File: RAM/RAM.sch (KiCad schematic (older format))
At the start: 15 parts, among them J1 Conn_01x08_Male, J2 Conn_01x08_Male, J3 Conn_01x08_Male, J4 Conn_01x05_Male, J5 Conn_01x08_Male, U1 74LS283, U2 CY62256-70PC, U3 74LS283, U4 74LS283, U5 74LS283

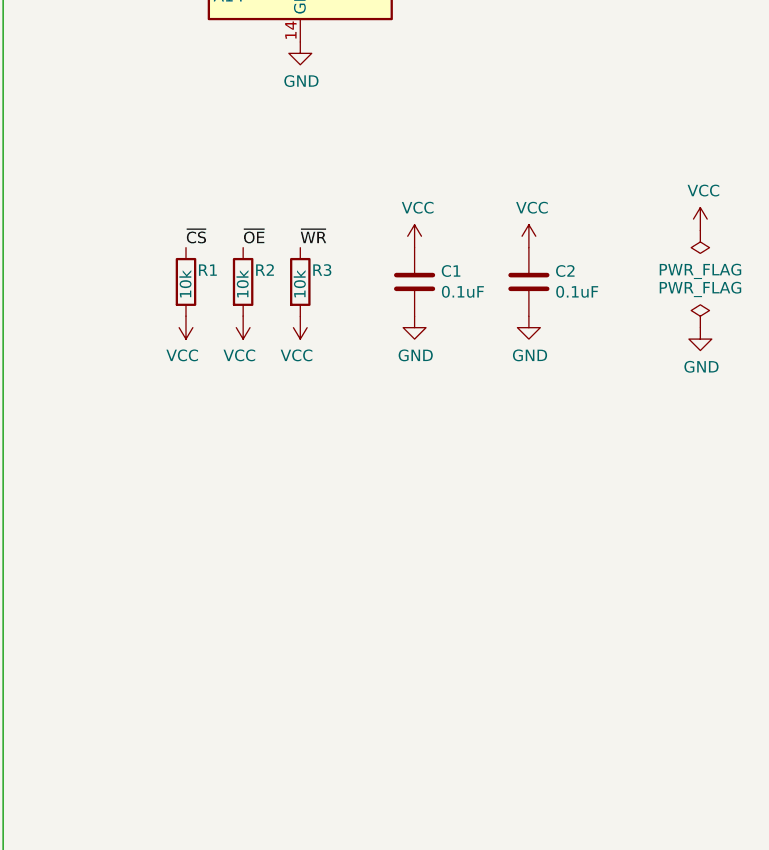
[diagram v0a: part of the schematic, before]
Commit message: Polishing RAM
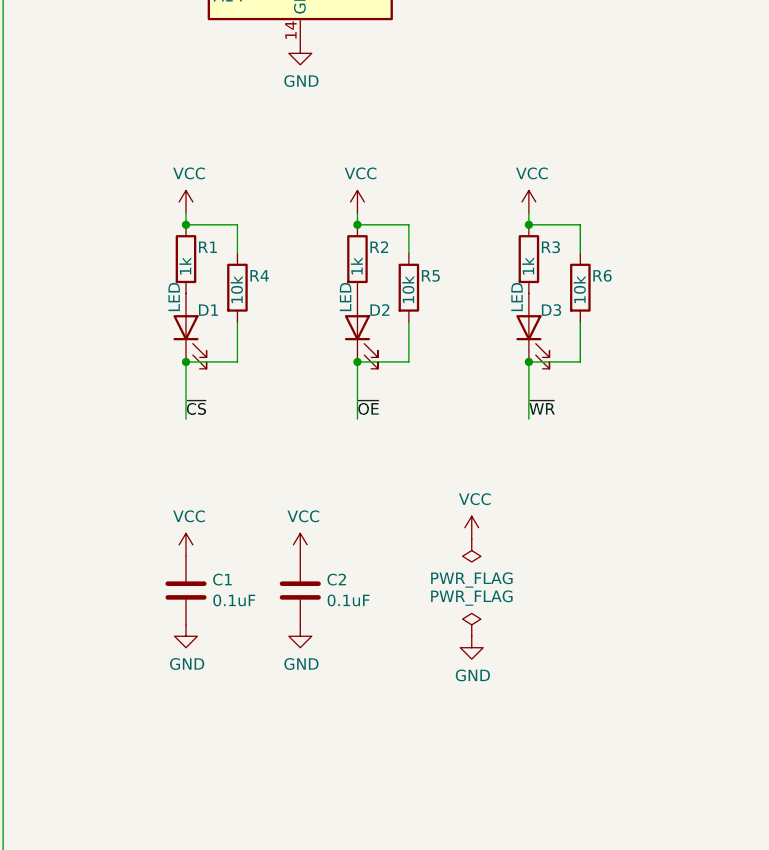
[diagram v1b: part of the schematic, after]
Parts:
- added D1, D2, D3: LED, LED_SMD:LED_0805_2012Metric_Pad1.15x1.40mm_HandSolder, symbol Device:LED
- added R4, R5, R6: 10k, Resistor_SMD:R_0805_2012Metric_Pad1.20x1.40mm_HandSolder, symbol Device:R
- R1, R2, R3: value 10k -> 1k
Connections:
- net VCC: now also R1.1, R2.1, R3.1, R4.1, R5.1, R6.1; no longer R1.2, R2.2, R3.2
- net ~CS: now also D1.1 (K), R4.2; no longer R1.1
- net ~OE: now also D2.1 (K), R5.2; no longer R2.1
- net ~WR: now also D3.1 (K), R6.2; no longer R3.1
- new net: D1.2 (A), R1.2
- new net: D2.2 (A), R2.2
- new net: D3.2 (A), R3.2
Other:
- moved on the sheet: C1, C2, R1, R2, R3

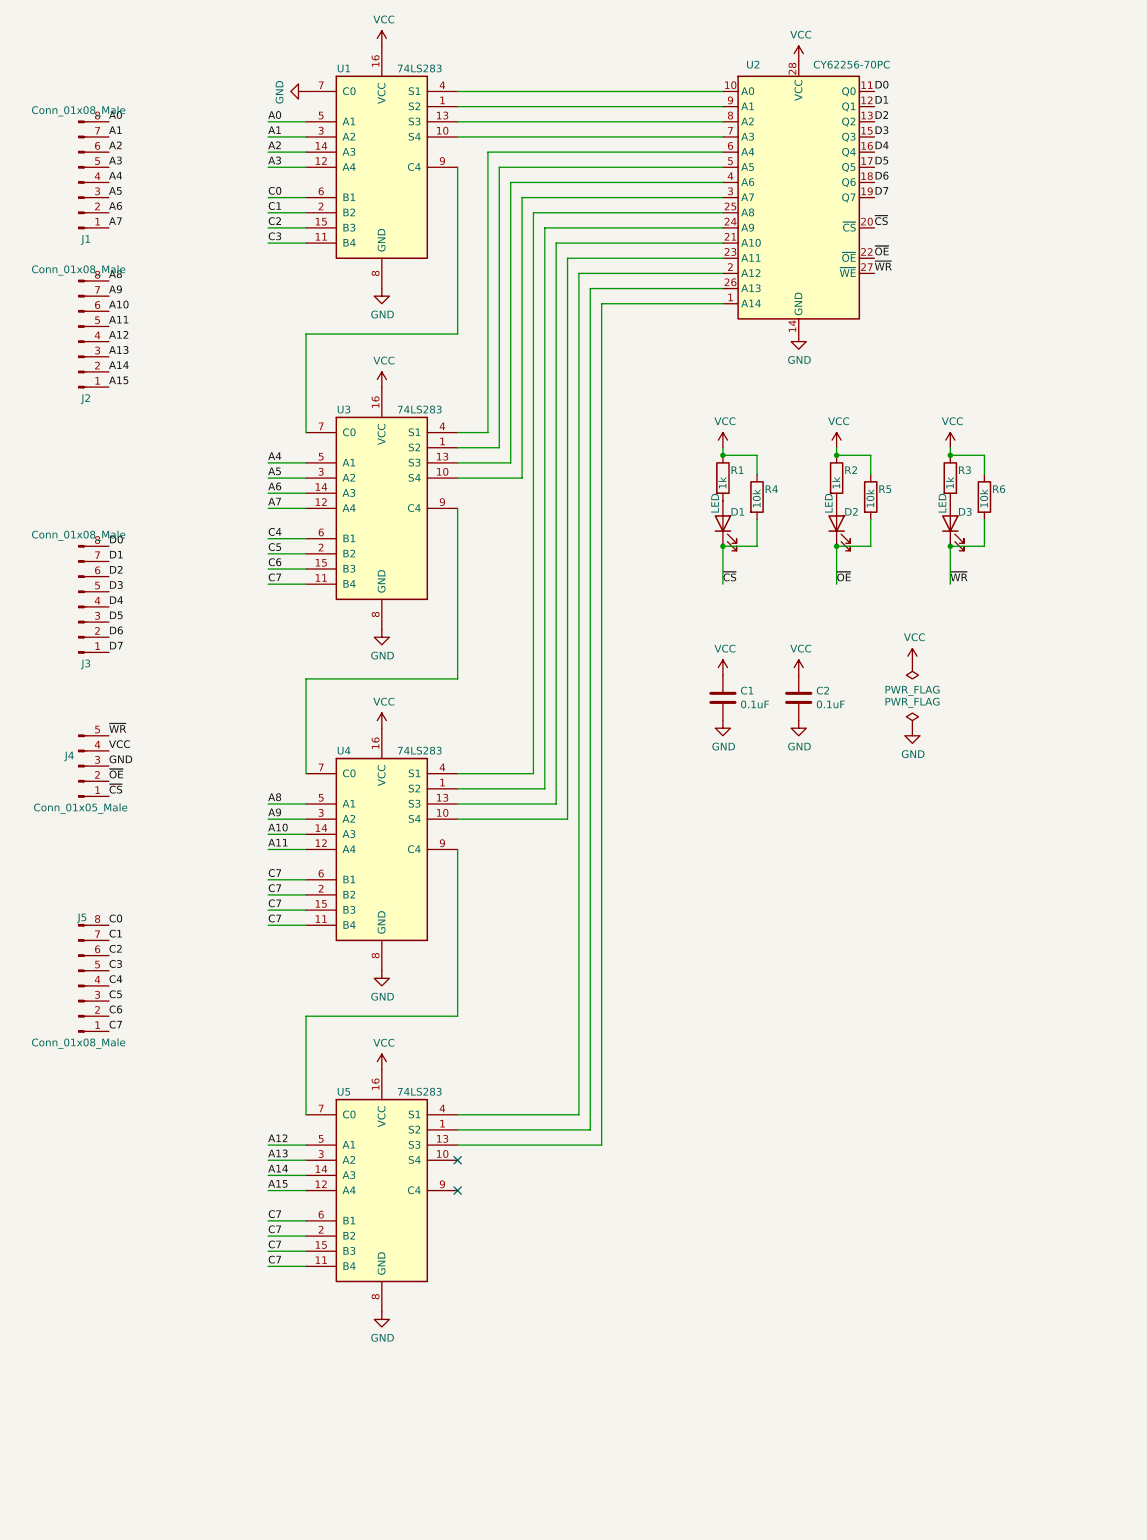
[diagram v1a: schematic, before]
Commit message: Try to add ROM to RAM
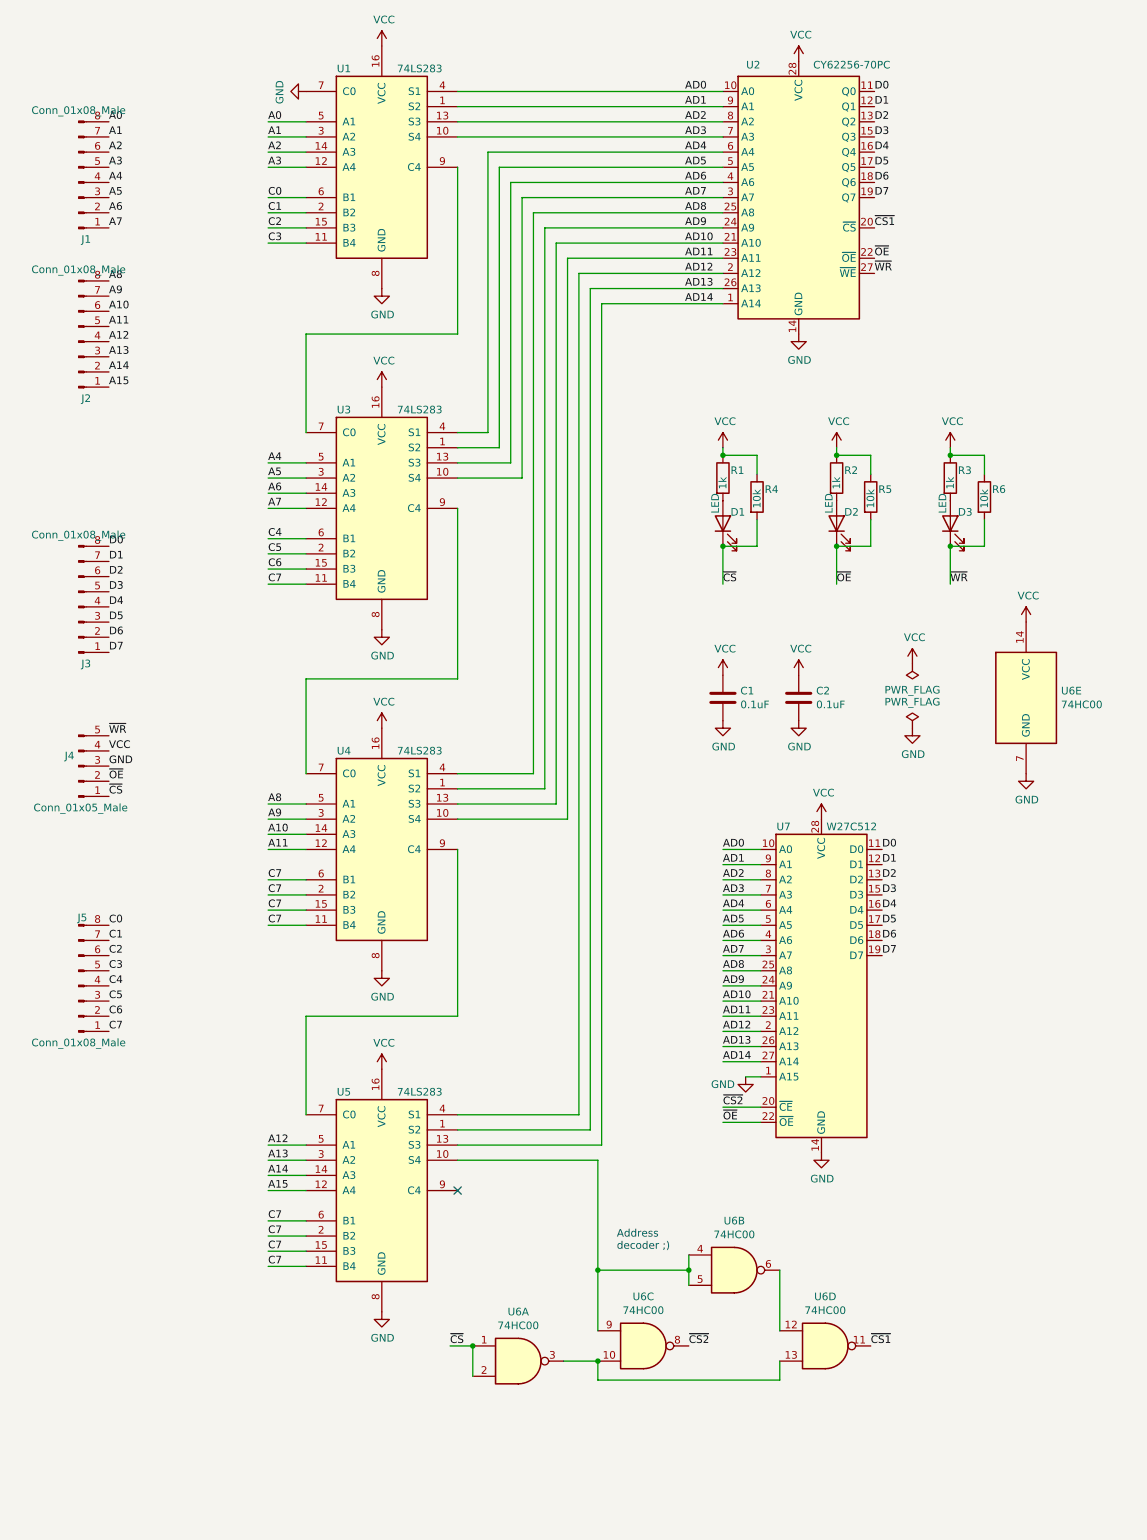
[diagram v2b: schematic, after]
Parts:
- added U6: 74HC00, Package_DIP:DIP-14_W7.62mm, symbol 74xx:74HC00
- added U7: W27C512, Package_DIP:DIP-28_W15.24mm, symbol Memory_EPROM:27C512
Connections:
- net D0: now also U7.11 (D0)
- net D1: now also U7.12 (D1)
- net D2: now also U7.13 (D2)
- net D3: now also U7.15 (D3)
- net D4: now also U7.16 (D4)
- net D5: now also U7.17 (D5)
- net D6: now also U7.18 (D6)
- net D7: now also U7.19 (D7)
- net GND: now also U6.7 (GND), U7.1 (A15), U7.14 (GND)
- net VCC: now also U6.14 (VCC), U7.28 (VCC)
- net ~CS: now also U6.1, U6.2; no longer U2.20 (~CS)
- net ~OE: now also U7.22 (~OE)
- net AD14: now reaches U2.1 (A14), U5.13 (S3)
- net AD14: now also U7.27 (A14)
- net AD0: now reaches U1.4 (S1), U2.10 (A0)
- net AD0: now also U7.10 (A0)
- net AD12: now reaches U2.2 (A12), U5.4 (S1)
- net AD12: now also U7.2 (A12)
- net AD10: now reaches U2.21 (A10), U4.13 (S3)
- net AD10: now also U7.21 (A10)
- net AD11: now reaches U2.23 (A11), U4.10 (S4)
- net AD11: now also U7.23 (A11)
- net AD9: now reaches U2.24 (A9), U4.1 (S2)
- net AD9: now also U7.24 (A9)
- net AD8: now reaches U2.25 (A8), U4.4 (S1)
- net AD8: now also U7.25 (A8)
- net AD13: now reaches U2.26 (A13), U5.1 (S2)
- net AD13: now also U7.26 (A13)
- net AD7: now reaches U2.3 (A7), U3.10 (S4)
- net AD7: now also U7.3 (A7)
- net AD6: now reaches U2.4 (A6), U3.13 (S3)
- net AD6: now also U7.4 (A6)
- net AD5: now reaches U2.5 (A5), U3.1 (S2)
- net AD5: now also U7.5 (A5)
- net AD4: now reaches U2.6 (A4), U3.4 (S1)
- net AD4: now also U7.6 (A4)
- net AD3: now reaches U1.10 (S4), U2.7 (A3)
- net AD3: now also U7.7 (A3)
- net AD2: now reaches U1.13 (S3), U2.8 (A2)
- net AD2: now also U7.8 (A2)
- net AD1: now reaches U1.1 (S2), U2.9 (A1)
- net AD1: now also U7.9 (A1)
- net at U5.10 (S4): now also U6.4, U6.5, U6.9
- new net: U6.10, U6.13, U6.3
- new net: U6.12, U6.6
- new net ~CS1: U2.20 (~CS), U6.11
- new net ~CS2: U6.8, U7.20 (~CE)
- no-connect marks 2 -> 1
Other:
- note added: "Address\ndecoder ;)"

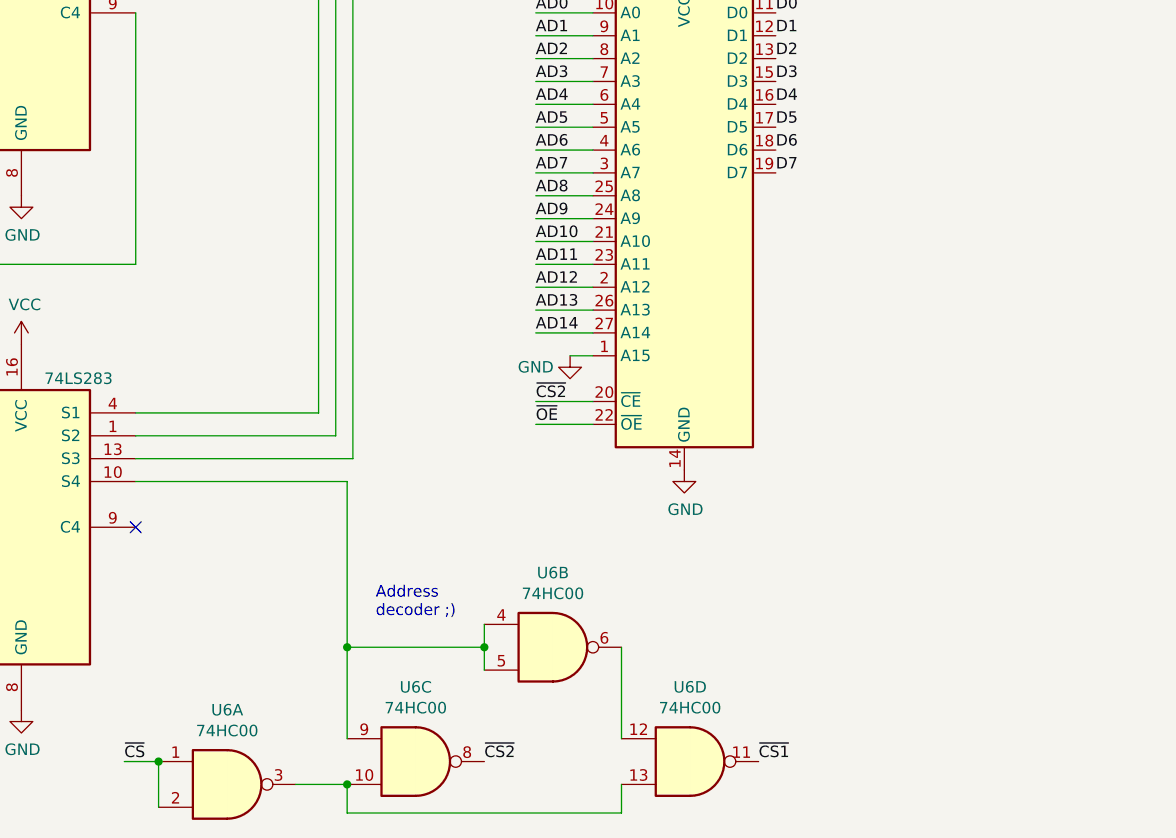
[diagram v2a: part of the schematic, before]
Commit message: Try to add ROM to RAM
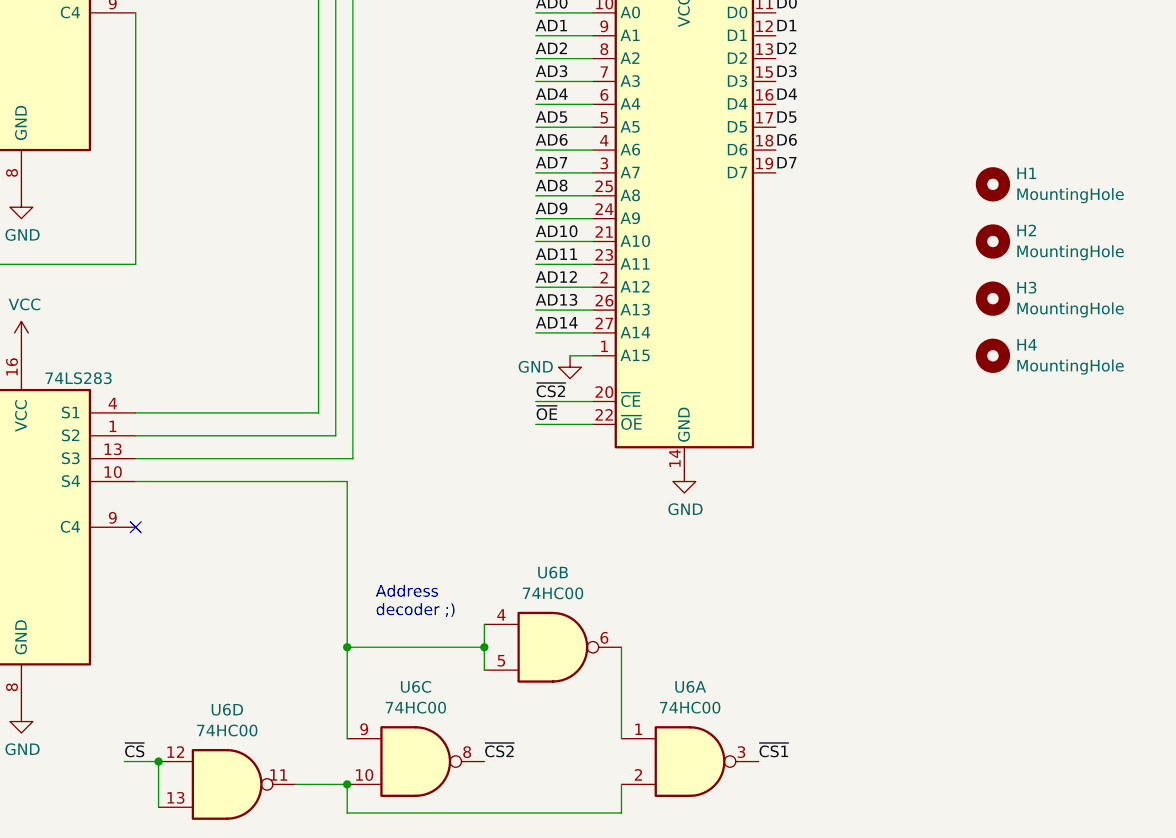
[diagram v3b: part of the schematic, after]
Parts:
- added H1, H2, H3, H4: MountingHole, MountingHole:MountingHole_3.2mm_M3, symbol Mechanical:MountingHole
- D1, D2, D3: footprint LED_SMD:LED_0805_2012Metric_Pad1.15x1.40mm_HandSolder -> LED_THT:LED_Rectangular_W5.0mm_H2.0mm
- J1, J2, J3: footprint Connector_PinHeader_2.54mm:PinHeader_1x08_P2.54mm_Horizontal -> Connector_PinHeader_2.54mm:PinHeader_1x08_P2.54mm_Vertical
- J4: footprint Connector_PinHeader_2.54mm:PinHeader_1x05_P2.54mm_Horizontal -> Connector_PinHeader_2.54mm:PinHeader_1x05_P2.54mm_Vertical
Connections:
- net ~CS: now also U6.12, U6.13; no longer U6.1, U6.2
- net ~CS1: now also U6.3; no longer U6.11
- net at U6.6: now also U6.1; no longer U6.12
- new net: U6.10, U6.11, U6.2
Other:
- moved on the sheet: U6A, U6D
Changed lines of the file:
@@
 F 0 "J1" H 800 2225 50  0000 C CNN
 F 1 "Conn_01x08_Male" H 750 1375 50  0000 C CNN
-F 2 "Connector_PinHeader_2.54mm:PinHeader_1x08_P2.54mm_Horizontal" H 750 1850 50  0001 C CNN
+F 2 "Connector_PinHeader_2.54mm:PinHeader_1x08_P2.54mm_Vertical" H 750 1850 50  0001 C CNN
 F 3 "~" H 750 1850 50  0001 C CNN
 	1    750  1850
@@
 F 0 "J2" H 800 3275 50  0000 C CNN
 F 1 "Conn_01x08_Male" H 750 2425 50  0000 C CNN
-F 2 "Connector_PinHeader_2.54mm:PinHeader_1x08_P2.54mm_Horizontal" H 750 2900 50  0001 C CNN
+F 2 "Connector_PinHeader_2.54mm:PinHeader_1x08_P2.54mm_Vertical" H 750 2900 50  0001 C CNN
 F 3 "~" H 750 2900 50  0001 C CNN
 	1    750  2900
@@
 F 0 "J3" H 800 5025 50  0000 C CNN
 F 1 "Conn_01x08_Male" H 750 4175 50  0000 C CNN
-F 2 "Connector_PinHeader_2.54mm:PinHeader_1x08_P2.54mm_Horizontal" H 750 4650 50  0001 C CNN
+F 2 "Connector_PinHeader_2.54mm:PinHeader_1x08_P2.54mm_Vertical" H 750 4650 50  0001 C CNN
 F 3 "~" H 750 4650 50  0001 C CNN
 	1    750  4650
@@
 F 0 "J4" H 722 5632 50  0000 R CNN
 F 1 "Conn_01x05_Male" H 1075 5975 50  0000 R CNN
-F 2 "Connector_PinHeader_2.54mm:PinHeader_1x05_P2.54mm_Horizontal" H 750 5700 50  0001 C CNN
+F 2 "Connector_PinHeader_2.54mm:PinHeader_1x05_P2.54mm_Vertical" H 750 5700 50  0001 C CNN
 F 3 "~" H 750 5700 50  0001 C CNN
 	1    750  5700
@@
 F 0 "D1" V 5075 4050 50  0000 R CNN
 F 1 "LED" H 5200 4150 50  0000 R CNN
-F 2 "LED_SMD:LED_0805_2012Metric_Pad1.15x1.40mm_HandSolder" H 5000 4100 50  0001 C CNN
+F 2 "LED_THT:LED_Rectangular_W5.0mm_H2.0mm" H 5000 4100 50  0001 C CNN
 F 3 "~" H 5000 4100 50  0001 C CNN
 	1    5000 4100
@@
 F 0 "D2" V 5825 4050 50  0000 R CNN
 F 1 "LED" H 5950 4150 50  0000 R CNN
-F 2 "LED_SMD:LED_0805_2012Metric_Pad1.15x1.40mm_HandSolder" H 5750 4100 50  0001 C CNN
+F 2 "LED_THT:LED_Rectangular_W5.0mm_H2.0mm" H 5750 4100 50  0001 C CNN
 F 3 "~" H 5750 4100 50  0001 C CNN
 	1    5750 4100
@@
 F 0 "D3" V 6575 4050 50  0000 R CNN
 F 1 "LED" H 6700 4150 50  0000 R CNN
-F 2 "LED_SMD:LED_0805_2012Metric_Pad1.15x1.40mm_HandSolder" H 6500 4100 50  0001 C CNN
+F 2 "LED_THT:LED_Rectangular_W5.0mm_H2.0mm" H 6500 4100 50  0001 C CNN
 F 3 "~" H 6500 4100 50  0001 C CNN
 	1    6500 4100
@@
 L 74xx:74HC00 U6
 U 1 1 6495168F
-P 3650 9625
-F 0 "U6" H 3650 9950 50  0000 C CNN
-F 1 "74HC00" H 3650 9859 50  0000 C CNN
-F 2 "Package_DIP:DIP-14_W7.62mm" H 3650 9625 50  0001 C CNN
-F 3 "http://www.ti.com/lit/gpn/sn74hc00" H 3650 9625 50  0001 C CNN
-	1    3650 9625
+P 5675 9525
+F 0 "U6" H 5675 9850 50  0000 C CNN
+F 1 "74HC00" H 5675 9759 50  0000 C CNN
+F 2 "Package_DIP:DIP-14_W7.62mm" H 5675 9525 50  0001 C CNN
+F 3 "http://www.ti.com/lit/gpn/sn74hc00" H 5675 9525 50  0001 C CNN
+	1    5675 9525
 	1    0    0    -1
 $EndComp
@@
 L 74xx:74HC00 U6
 U 4 1 64956F5A
-P 5675 9525
-F 0 "U6" H 5675 9850 50  0000 C CNN
-F 1 "74HC00" H 5675 9759 50  0000 C CNN
-F 2 "Package_DIP:DIP-14_W7.62mm" H 5675 9525 50  0001 C CNN
-F 3 "http://www.ti.com/lit/gpn/sn74hc00" H 5675 9525 50  0001 C CNN
-	4    5675 9525
+P 3650 9625
+F 0 "U6" H 3650 9950 50  0000 C CNN
+F 1 "74HC00" H 3650 9859 50  0000 C CNN
+F 2 "Package_DIP:DIP-14_W7.62mm" H 3650 9625 50  0001 C CNN
+F 3 "http://www.ti.com/lit/gpn/sn74hc00" H 3650 9625 50  0001 C CNN
+	4    3650 9625
 	1    0    0    -1
 $EndComp
@@
 	4175 9750 5375 9750
 Wire Wire Line
-	5375 9750 5375 9625
-Wire Wire Line
 	3950 9625 4175 9625
 Connection ~ 4175 9625
@@
 Text Notes 4300 8900 0    50   ~ 0
 Address\ndecoder ;)
+$Comp
+L Mechanical:MountingHole H1
+U 1 1 64922E67
+P 7000 7000
+F 0 "H1" H 7100 7046 50  0000 L CNN
+F 1 "MountingHole" H 7100 6955 50  0000 L CNN
+F 2 "MountingHole:MountingHole_3.2mm_M3" H 7000 7000 50  0001 C CNN
+F 3 "~" H 7000 7000 50  0001 C CNN
+	1    7000 7000
+	1    0    0    -1
+$EndComp
+$Comp
+L Mechanical:MountingHole H2
+U 1 1 64923BB4
+P 7000 7250
+F 0 "H2" H 7100 7296 50  0000 L CNN
+F 1 "MountingHole" H 7100 7205 50  0000 L CNN
+F 2 "MountingHole:MountingHole_3.2mm_M3" H 7000 7250 50  0001 C CNN
+F 3 "~" H 7000 7250 50  0001 C CNN
+	1    7000 7250
+	1    0    0    -1
+$EndComp
+$Comp
+L Mechanical:MountingHole H3
+U 1 1 64924557
+P 7000 7500
+F 0 "H3" H 7100 7546 50  0000 L CNN
+F 1 "MountingHole" H 7100 7455 50  0000 L CNN
+F 2 "MountingHole:MountingHole_3.2mm_M3" H 7000 7500 50  0001 C CNN
+F 3 "~" H 7000 7500 50  0001 C CNN
+	1    7000 7500
+	1    0    0    -1
+$EndComp
+$Comp
+L Mechanical:MountingHole H4
+U 1 1 64924E63
+P 7000 7750
+F 0 "H4" H 7100 7796 50  0000 L CNN
+F 1 "MountingHole" H 7100 7705 50  0000 L CNN
+F 2 "MountingHole:MountingHole_3.2mm_M3" H 7000 7750 50  0001 C CNN
+F 3 "~" H 7000 7750 50  0001 C CNN
+	1    7000 7750
+	1    0    0    -1
+$EndComp
+Wire Wire Line
+	5375 9625 5375 9750
 $EndSCHEMATC
